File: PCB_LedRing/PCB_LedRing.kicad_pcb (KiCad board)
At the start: 2 copper layers, 60 x 60 mm, 62 parts, among them IC1 PCA9552D,118, J1 Conn_01x06

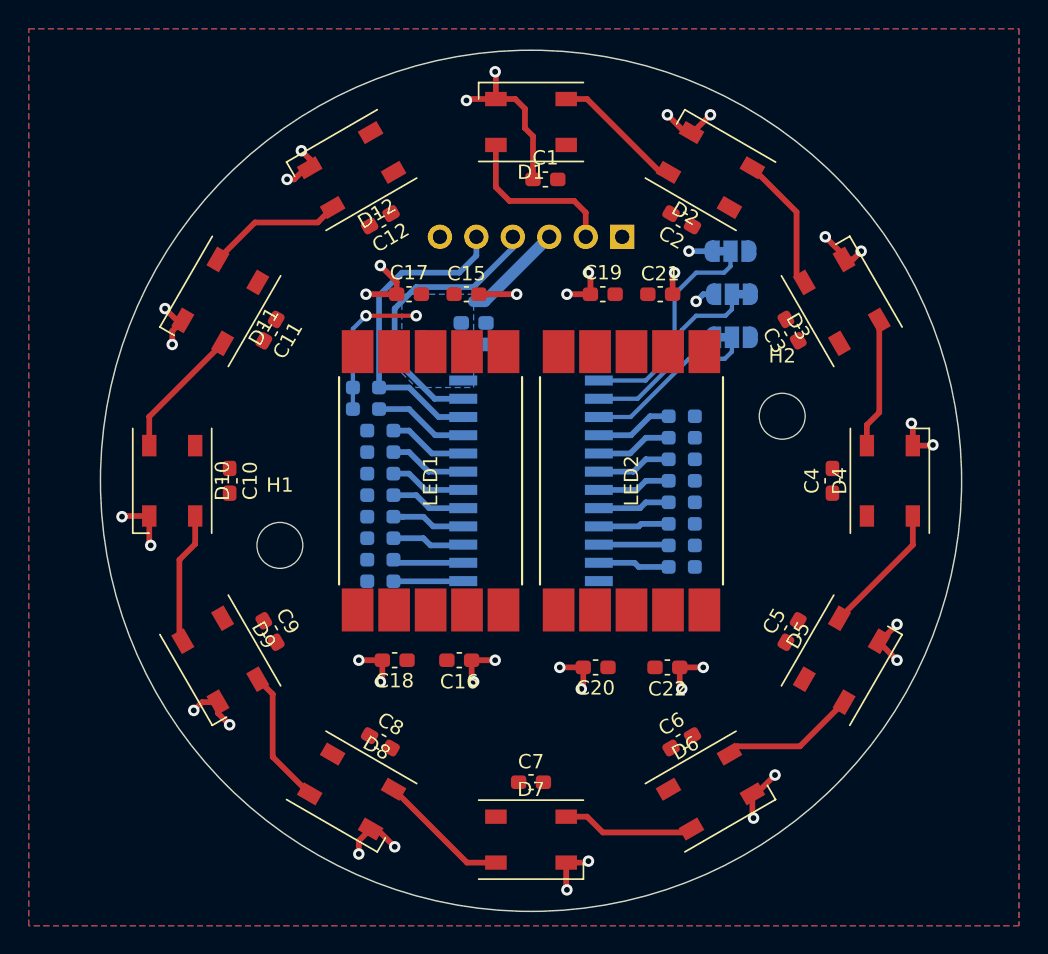
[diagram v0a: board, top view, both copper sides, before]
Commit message: Wire Digits and LEDs
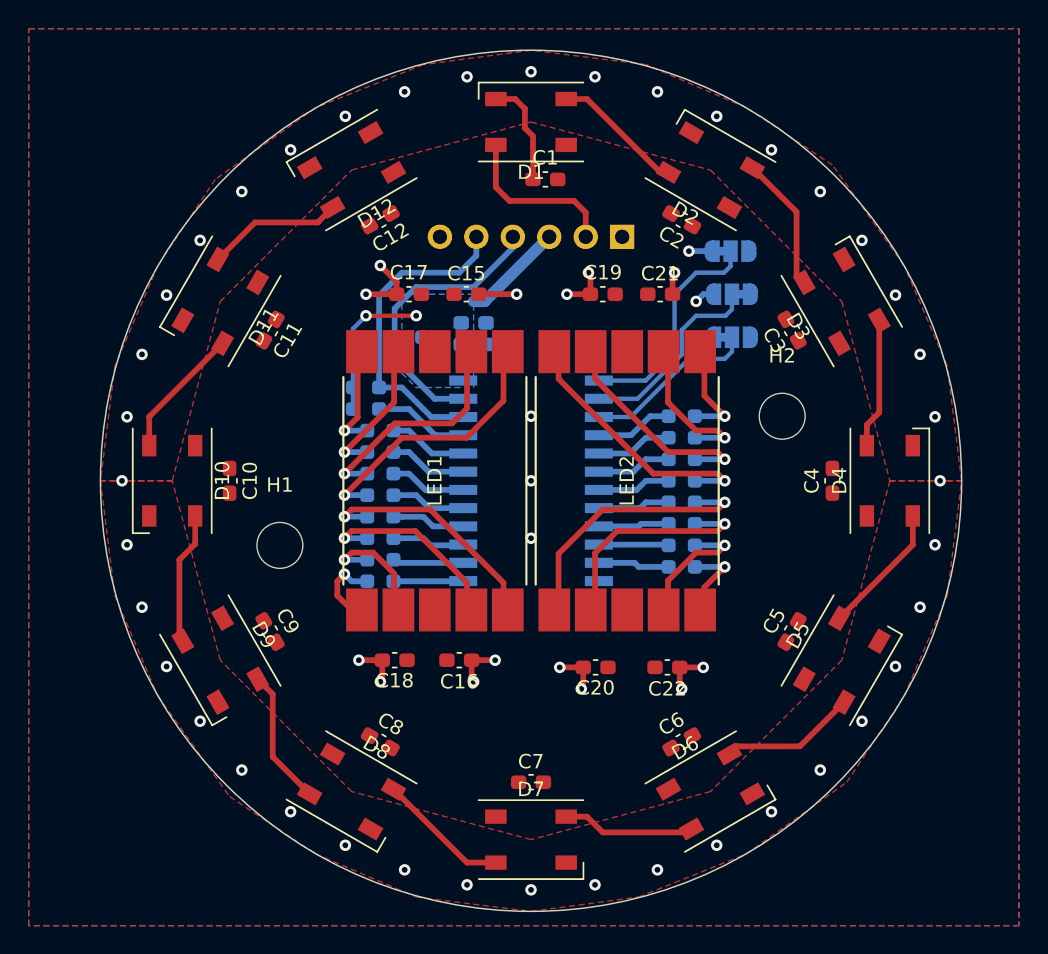
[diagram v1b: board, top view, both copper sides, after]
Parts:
- moved LED2 0.30 mm to (129.7, 93.0)
- moved LED1 0.30 mm to (116.3, 93.0)
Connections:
- R10 pad 2: /1DP -> /1G
- R12 pad 1: /2A -> /2B
- R13 pad 1: /2B -> /2A
- R14 pad 1: /2C -> /2F
- R15 pad 1: /2D -> /2G
- R17 pad 1: /2F -> /2D
- R18 pad 1: /2G -> /2C
- R3 pad 2: /1A -> /1E
- R4 pad 2: /1B -> /1D
- R6 pad 2: /1D -> /1DP
- R7 pad 2: /1E -> /1B
- R8 pad 2: /1F -> /1A
- R9 pad 2: /1G -> /1F
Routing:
- net GND: track 76.8 -> 34.1 mm, vias 38 -> 57
- net /2E: track 0.00 -> 19.1 mm, vias 0 -> 1
- net /1B: track 0.00 -> 18.8 mm, vias 0 -> 1
- net /2G: track 0.00 -> 18.5 mm, vias 0 -> 1
- net /1DP: track 0.00 -> 16.9 mm, vias 0 -> 1
- net /1A: track 0.00 -> 16.0 mm, vias 0 -> 1
- net /2D: track 0.00 -> 15.9 mm, vias 0 -> 1
- net /2F: track 0.00 -> 15.3 mm, vias 0 -> 1
- net /1C: track 0.00 -> 13.7 mm, vias 0 -> 1
- net /2A: track 0.00 -> 10.6 mm, vias 0 -> 1
- net /1F: track 0.00 -> 10.0 mm, vias 0 -> 1
- net /2C: track 0.00 -> 9.11 mm, vias 0 -> 1
- net /1D: track 0.00 -> 8.40 mm, vias 0 -> 1
- net /1G: track 0.00 -> 7.47 mm, vias 0 -> 1
- net /2B: track 0.00 -> 7.18 mm, vias 0 -> 1
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- added copper zone on F.Cu, net GND

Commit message: LED Board DRC
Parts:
- removed JP1, JP2, JP3: SolderJumper_3_Bridged12, Jumper:SolderJumper-3_P1.3mm_Bridged12_RoundedPad1.0x1.5mm_NumberLabels
- added H3: MountingHole, MountingHole:MountingHole_3.2mm_M3, F.Cu at (123.0, 109.5)
- added R20: 0, Resistor_SMD:R_0603_1608Metric_Pad0.98x0.95mm_HandSolder, B.Cu at (140.5, 80.0)
- added R21: 0, Resistor_SMD:R_0603_1608Metric_Pad0.98x0.95mm_HandSolder, B.Cu at (136.5, 80.0)
- added R22: 0, Resistor_SMD:R_0603_1608Metric_Pad0.98x0.95mm_HandSolder, B.Cu at (136.5, 81.5)
- added R23: 0, Resistor_SMD:R_0603_1608Metric_Pad0.98x0.95mm_HandSolder, B.Cu at (140.5, 81.5)
- added R24: 0, Resistor_SMD:R_0603_1608Metric_Pad0.98x0.95mm_HandSolder, B.Cu at (136.5, 84.5)
- added R25: 0, Resistor_SMD:R_0603_1608Metric_Pad0.98x0.95mm_HandSolder, B.Cu at (140.5, 84.5)
- added TP3: TestPoint, TestPoint:TestPoint_Pad_D3.0mm, B.Cu at (106.0, 94.0)
- added TP4: TestPoint, TestPoint:TestPoint_Pad_D3.0mm, B.Cu at (107.8, 77.2)
- R10, R12, R13, R14, R15, R16, R17, R18, R19, R3, R4, R5, R6, R7, R8, R9: value 82E -> 100
- moved H1 9.00 mm to (105.5, 88.5)
- moved R2 1.00 mm to (111.5, 85.5)
- moved R11 0.75 mm to (111.5, 87.2)
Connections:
- net Net-(IC1-~{RESET}) renamed /RESET
- D1 pad 2: /LED -> Net-(D1-DIN)
- D1 pad 4: Net-(D1-DOUT) -> unconnected-(D1-DOUT-Pad4)
- D12 pad 4: unconnected-(D12-DOUT-Pad4) -> Net-(D1-DIN)
- D2 pad 2: Net-(D1-DOUT) -> /LED
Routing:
- net GND: track 34.1 -> 90.0 mm, vias 57 -> 80
- net VCC: track 20.5 -> 34.2 mm, vias 4 -> 5
- net /RESET: track 6.62 -> 17.8 mm
- net Net-(D1-DOUT): track 9.24 -> 0.00 mm
- net Net-(D1-DIN): track 0.00 -> 9.08 mm
- net /A2: track 12.2 -> 15.8 mm
- net /LED: track 11.6 -> 9.11 mm
- net /A1: track 13.9 -> 15.9 mm
- net /2A: track 10.6 -> 12.3 mm
- net /1B: track 18.8 -> 17.6 mm
- net /1A: track 16.0 -> 14.8 mm
- net /A0: track 15.9 -> 15.2 mm
- net /SCL: track 22.4 -> 21.8 mm

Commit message: Change connector
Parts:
- added G***: LOGO, LOGO, B.Cu at (106.5, 105.5)
- J1: value Conn_01x06 -> Board2Board; footprint Connector_PinHeader_2.54mm:PinHeader_1x06_P2.54mm_Vertical -> Connector_PinHeader_2.54mm:PinHeader_2x03_P2.54mm_Vertical_SMD
- R10, R12, R13, R14, R15, R16, R17, R18, R19, R3, R4, R5, R6, R7, R8, R9: value 100 -> 270
- moved J1 1.92 mm to (127.5, 75.5)
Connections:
- C13 pad 1: VCC -> +3V3
- C14 pad 1: VCC -> +3V3
- IC1 pad 24: VCC -> +3V3
- J1 pad 3: VCC -> +3V3
- J1 pad 4: /SDA -> VCC
- J1 pad 5: /SCL -> /SDA
- J1 pad 6: GND -> /SCL
- R1 pad 1: VCC -> +3V3
- R11 pad 1: VCC -> +3V3
- R2 pad 1: VCC -> +3V3
- R21 pad 2: VCC -> +3V3
- R22 pad 2: VCC -> +3V3
- R24 pad 2: VCC -> +3V3
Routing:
- net +3V3: track 0.00 -> 42.3 mm, vias 0 -> 4
- net GND: track 90.0 -> 117.4 mm, vias 80 -> 89
- net VCC: track 34.2 -> 22.9 mm, vias 5 -> 3
- net /SCL: track 21.8 -> 28.0 mm
- net /LED: track 9.11 -> 5.05 mm, vias 0 -> 1
- net /SDA: track 20.2 -> 22.6 mm
- added copper zone on B.Cu, net +3V3
- removed copper zone on B.Cu, net VCC
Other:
- board text added: "GND 3V3 SDA"
- board text added: "LED VCC SCL"
- board text removed: "GND LED VCC SDA SCL GND"

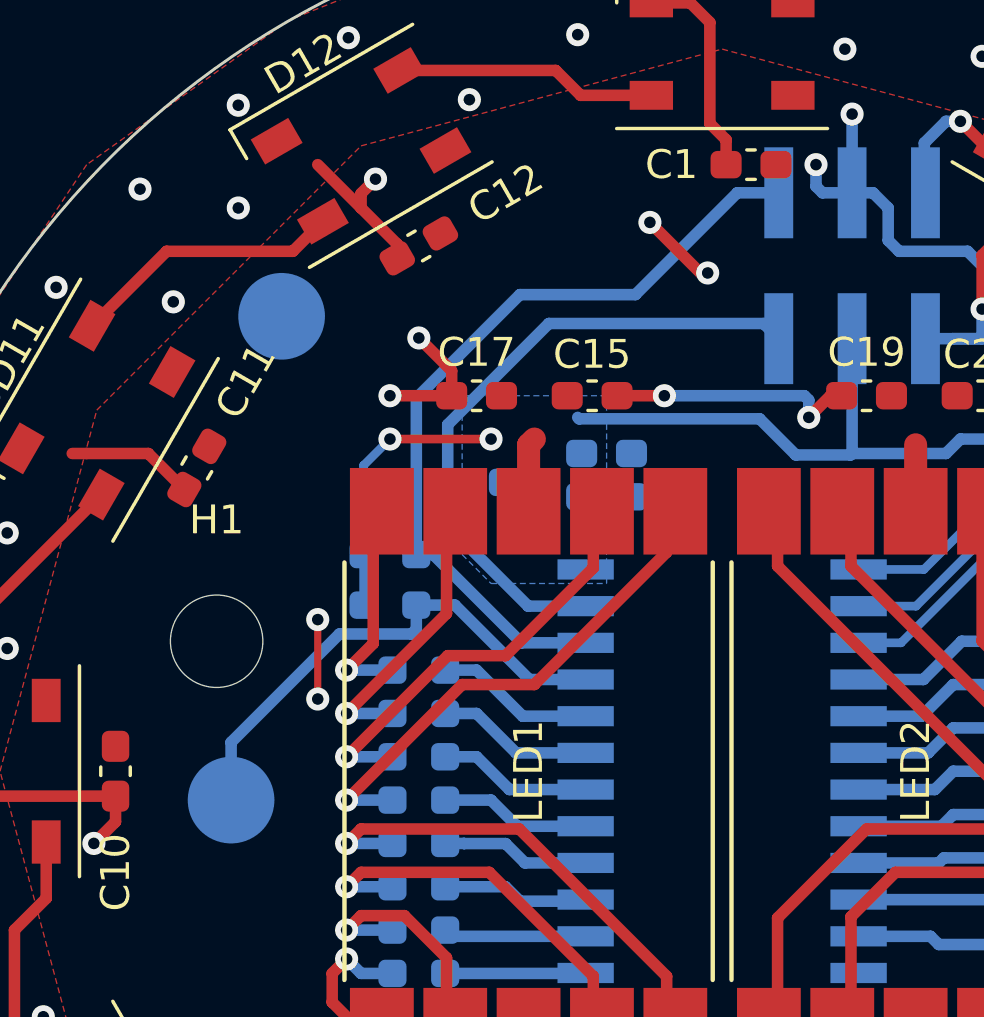
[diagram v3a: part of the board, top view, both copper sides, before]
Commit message: Update LED ring based on review
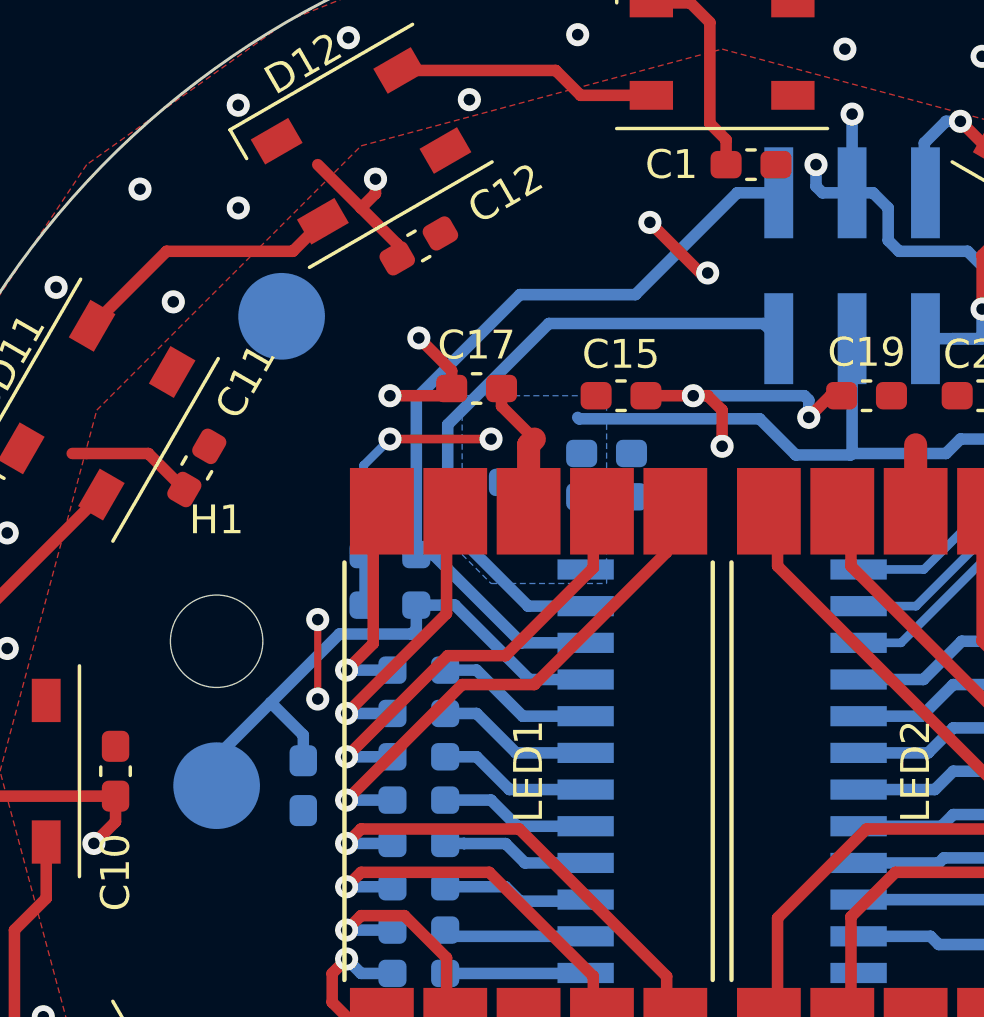
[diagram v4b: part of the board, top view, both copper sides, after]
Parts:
- added C23: 100n, Capacitor_SMD:C_0603_1608Metric_Pad1.08x0.95mm_HandSolder, B.Cu at (108.5, 93.5)
- H1, H2, H3: value MountingHole -> MountingHole M3
- R10, R12, R13, R14, R15, R16, R17, R18, R19, R3, R4, R5, R6, R7, R8, R9: value 270 -> 330
- moved C15 1.00 mm to (119.5, 80.0)
- moved TP3 0.71 mm to (105.5, 93.5)
- moved C17 0.25 mm to (114.5, 79.8)
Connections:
- net /LED renamed /LED_DI
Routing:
- net VCC: track 22.9 -> 25.1 mm
- net /RESET: track 17.8 -> 20.0 mm
- net GND: track 117.4 -> 118.8 mm, vias 89 -> 90

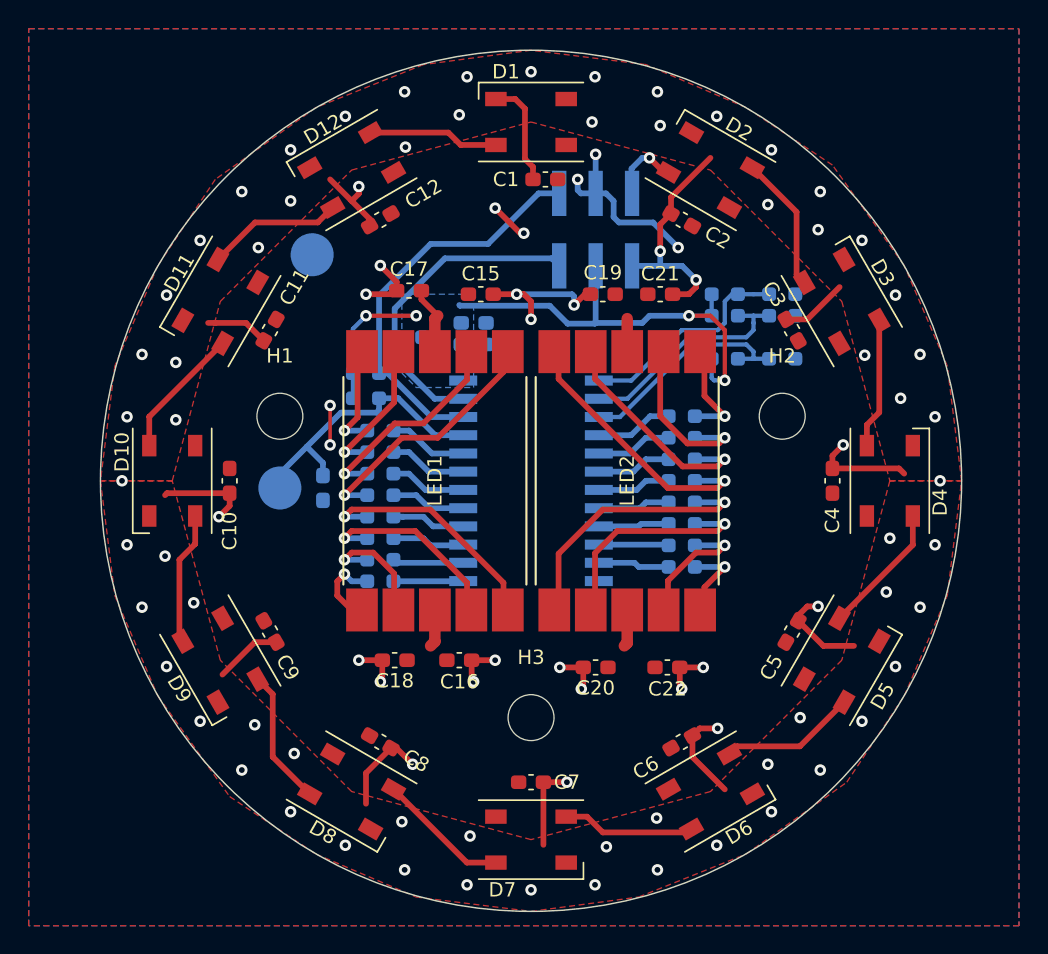
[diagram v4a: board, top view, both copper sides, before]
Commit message: Add Level Shifter
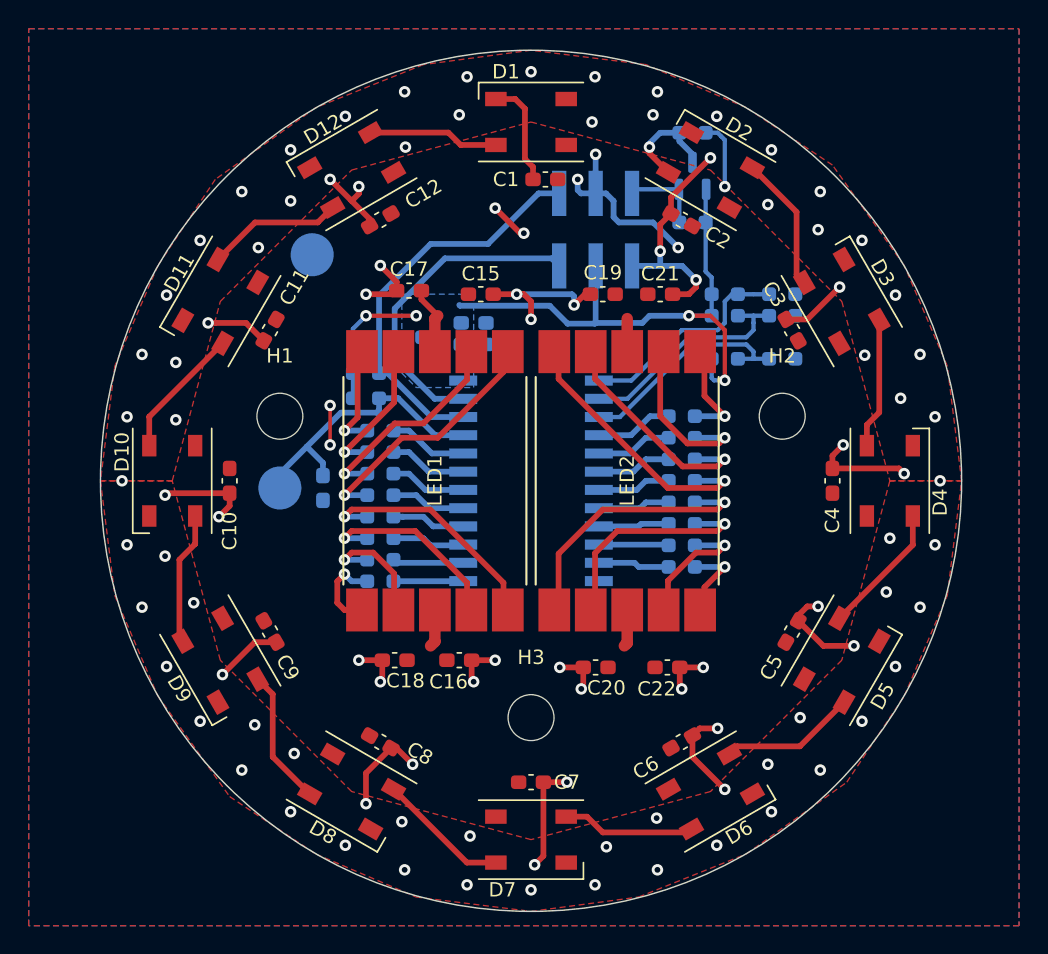
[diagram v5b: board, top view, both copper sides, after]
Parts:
- added Q1: BSS138, Package_TO_SOT_SMD:SOT-23, B.Cu at (134.2, 71.8)
- added R26: 10k, Resistor_SMD:R_0603_1608Metric_Pad0.98x0.95mm_HandSolder, B.Cu at (134.2, 75.0)
- added R27: 10k, Resistor_SMD:R_0603_1608Metric_Pad0.98x0.95mm_HandSolder, B.Cu at (134.2, 68.8)
- added REF**: KiCad-Logo2_8mm_SilkScreen, Symbol:KiCad-Logo2_8mm_SilkScreen, B.Cu at (135.8, 104.4)
- C13: value 100n -> 4.7u
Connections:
- D2 pad 2: /LED_DI -> /LED_DI_HV
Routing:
- net +3V3: track 42.3 -> 49.8 mm
- net /LED_DI_HV: track 0.00 -> 7.40 mm, vias 0 -> 1
- net VCC: track 25.1 -> 29.9 mm, vias 3 -> 4
- net GND: track 118.8 -> 120.4 mm, vias 90 -> 101
- net /LED_DI: track 5.05 -> 5.76 mm, vias 1 -> 0
